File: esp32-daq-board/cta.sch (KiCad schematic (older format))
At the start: 27 parts, among them J2 Conn_01x15_Female, J3 Conn_01x15_Female

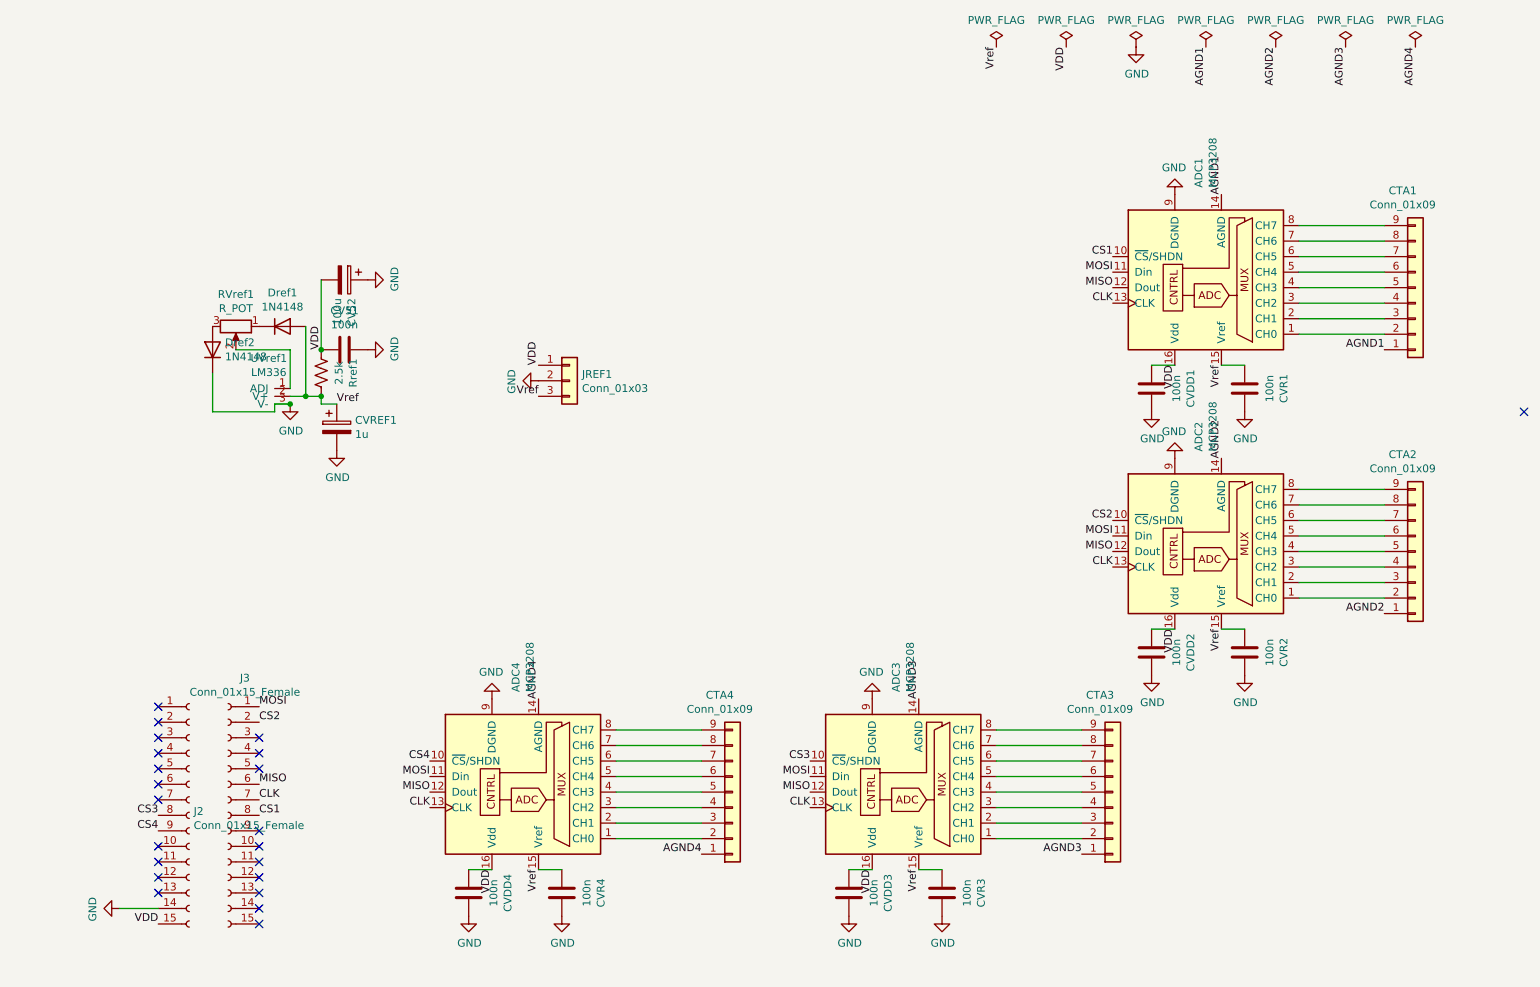
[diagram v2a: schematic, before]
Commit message: Unifying all the grounds AGND and DGND
On the previous version, each anemometer had a ground that was connected to the AGND present in the MCP3208. This was burning the MCP3208. I still need to undersant how to work with this AGND properly.
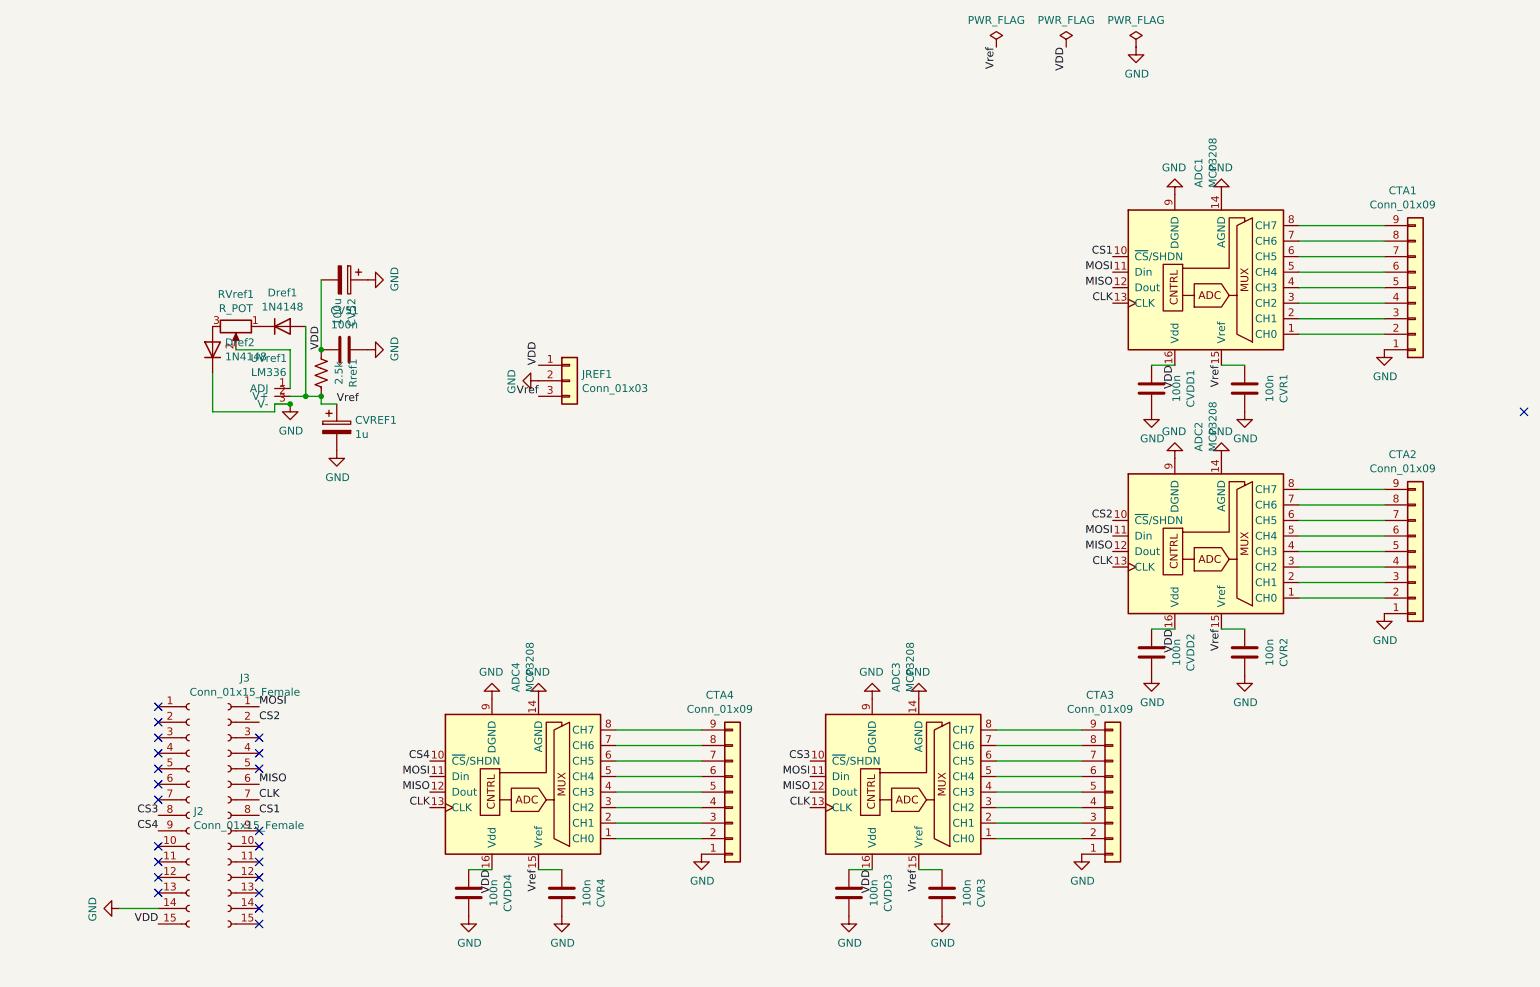
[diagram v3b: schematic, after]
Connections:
- net AGND1 is gone; now on net GND: ADC1.14 (AGND), CTA1.1 (Pin_1)
- net AGND2 is gone; now on net GND: ADC2.14 (AGND), CTA2.1 (Pin_1)
- net AGND3 is gone; now on net GND: ADC3.14 (AGND), CTA3.1 (Pin_1)
- net AGND4 is gone; now on net GND: ADC4.14 (AGND), CTA4.1 (Pin_1)
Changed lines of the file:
@@
 Text Label 1900 6600 2    50   ~ 0
 VDD
-Text Label 8650 950  3    50   ~ 0
-AGND1
-$Comp
-L power:PWR_FLAG #FLG0101
-U 1 1 60C44B26
-P 8650 950
-F 0 "#FLG0101" H 8650 1025 50  0001 C CNN
-F 1 "PWR_FLAG" H 8650 1123 50  0000 C CNN
-F 2 "" H 8650 950 50  0001 C CNN
-F 3 "~" H 8650 950 50  0001 C CNN
-	1    8650 950
-	1    0    0    -1
-$EndComp
-Text Label 10000 950  3    50   ~ 0
-AGND4
-$Comp
-L power:PWR_FLAG #FLG0104
-U 1 1 60C484D7
-P 9100 950
-F 0 "#FLG0104" H 9100 1025 50  0001 C CNN
-F 1 "PWR_FLAG" H 9100 1123 50  0000 C CNN
-F 2 "" H 9100 950 50  0001 C CNN
-F 3 "~" H 9100 950 50  0001 C CNN
-	1    9100 950
-	1    0    0    -1
-$EndComp
-Text Label 9100 950  3    50   ~ 0
-AGND2
-$Comp
-L power:PWR_FLAG #FLG0105
-U 1 1 60C48AD3
-P 9550 950
-F 0 "#FLG0105" H 9550 1025 50  0001 C CNN
-F 1 "PWR_FLAG" H 9550 1123 50  0000 C CNN
-F 2 "" H 9550 950 50  0001 C CNN
-F 3 "~" H 9550 950 50  0001 C CNN
-	1    9550 950
-	1    0    0    -1
-$EndComp
-$Comp
-L power:PWR_FLAG #FLG0106
-U 1 1 60C4A046
-P 10000 950
-F 0 "#FLG0106" H 10000 1025 50  0001 C CNN
-F 1 "PWR_FLAG" H 10000 1123 50  0000 C CNN
-F 2 "" H 10000 950 50  0001 C CNN
-F 3 "~" H 10000 950 50  0001 C CNN
-	1    10000 950
-	1    0    0    -1
-$EndComp
-Text Label 9550 950  3    50   ~ 0
-AGND3
-Text Label 8750 1900 1    50   ~ 0
-AGND1
-Text Label 8750 3600 1    50   ~ 0
-AGND2
-Text Label 6800 5150 1    50   ~ 0
-AGND3
-Text Label 4350 5150 1    50   ~ 0
-AGND4
 $Comp
 L Connector_Generic:Conn_01x09 CTA1
@@
 	1    0    0    1
 $EndComp
-Text Label 9800 2900 2    50   ~ 0
-AGND1
 $Comp
 L Connector_Generic:Conn_01x09 CTA2
@@
 	1    0    0    1
 $EndComp
-Text Label 9800 4600 2    50   ~ 0
-AGND2
 $Comp
 L Connector_Generic:Conn_01x09 CTA3
@@
 	1    0    0    1
 $EndComp
-Text Label 7850 6150 2    50   ~ 0
-AGND3
 $Comp
 L Connector_Generic:Conn_01x09 CTA4
@@
 	1    0    0    1
 $EndComp
-Text Label 5400 6150 2    50   ~ 0
-AGND4
 $Comp
 L power:PWR_FLAG #FLG0107
@@
 Text Label 4350 3000 1    50   ~ 0
 VDD
+$Comp
+L power:GND #PWR0105
+U 1 1 60CB532B
+P 8750 3600
+F 0 "#PWR0105" H 8750 3350 50  0001 C CNN
+F 1 "GND" H 8755 3427 50  0000 C CNN
+F 2 "" H 8750 3600 50  0001 C CNN
+F 3 "" H 8750 3600 50  0001 C CNN
+	1    8750 3600
+	-1   0    0    1
+$EndComp
+$Comp
+L power:GND #PWR0106
+U 1 1 60CB653E
+P 8750 1900
+F 0 "#PWR0106" H 8750 1650 50  0001 C CNN
+F 1 "GND" H 8755 1727 50  0000 C CNN
+F 2 "" H 8750 1900 50  0001 C CNN
+F 3 "" H 8750 1900 50  0001 C CNN
+	1    8750 1900
+	-1   0    0    1
+$EndComp
+$Comp
+L power:GND #PWR0109
+U 1 1 60CB8E9D
+P 6800 5150
+F 0 "#PWR0109" H 6800 4900 50  0001 C CNN
+F 1 "GND" H 6805 4977 50  0000 C CNN
+F 2 "" H 6800 5150 50  0001 C CNN
+F 3 "" H 6800 5150 50  0001 C CNN
+	1    6800 5150
+	-1   0    0    1
+$EndComp
+$Comp
+L power:GND #PWR0110
+U 1 1 60CBA52D
+P 4350 5150
+F 0 "#PWR0110" H 4350 4900 50  0001 C CNN
+F 1 "GND" H 4355 4977 50  0000 C CNN
+F 2 "" H 4350 5150 50  0001 C CNN
+F 3 "" H 4350 5150 50  0001 C CNN
+	1    4350 5150
+	-1   0    0    1
+$EndComp
+$Comp
+L power:GND #PWR?
+U 1 1 60CC55EC
+P 9800 2900
+F 0 "#PWR?" H 9800 2650 50  0001 C CNN
+F 1 "GND" H 9805 2727 50  0000 C CNN
+F 2 "" H 9800 2900 50  0001 C CNN
+F 3 "" H 9800 2900 50  0001 C CNN
+	1    9800 2900
+	1    0    0    -1
+$EndComp
+$Comp
+L power:GND #PWR?
+U 1 1 60CC5D37
+P 7850 6150
+F 0 "#PWR?" H 7850 5900 50  0001 C CNN
+F 1 "GND" H 7855 5977 50  0000 C CNN
+F 2 "" H 7850 6150 50  0001 C CNN
+F 3 "" H 7850 6150 50  0001 C CNN
+	1    7850 6150
+	1    0    0    -1
+$EndComp
+$Comp
+L power:GND #PWR?
+U 1 1 60CC69A8
+P 9800 4600
+F 0 "#PWR?" H 9800 4350 50  0001 C CNN
+F 1 "GND" H 9805 4427 50  0000 C CNN
+F 2 "" H 9800 4600 50  0001 C CNN
+F 3 "" H 9800 4600 50  0001 C CNN
+	1    9800 4600
+	1    0    0    -1
+$EndComp
+$Comp
+L power:GND #PWR?
+U 1 1 60CD17FA
+P 5400 6150
+F 0 "#PWR?" H 5400 5900 50  0001 C CNN
+F 1 "GND" H 5405 5977 50  0000 C CNN
+F 2 "" H 5400 6150 50  0001 C CNN
+F 3 "" H 5400 6150 50  0001 C CNN
+	1    5400 6150
+	1    0    0    -1
+$EndComp
 $EndSCHEMATC
